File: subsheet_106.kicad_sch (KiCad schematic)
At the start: 59 parts, among them P01 1K, Q01 16MHz, T04 BC557B, T05 BC337-40, T06 BC547B, T07 BC547B, T08 BC557B, T09 BC547B, T10 BC547B

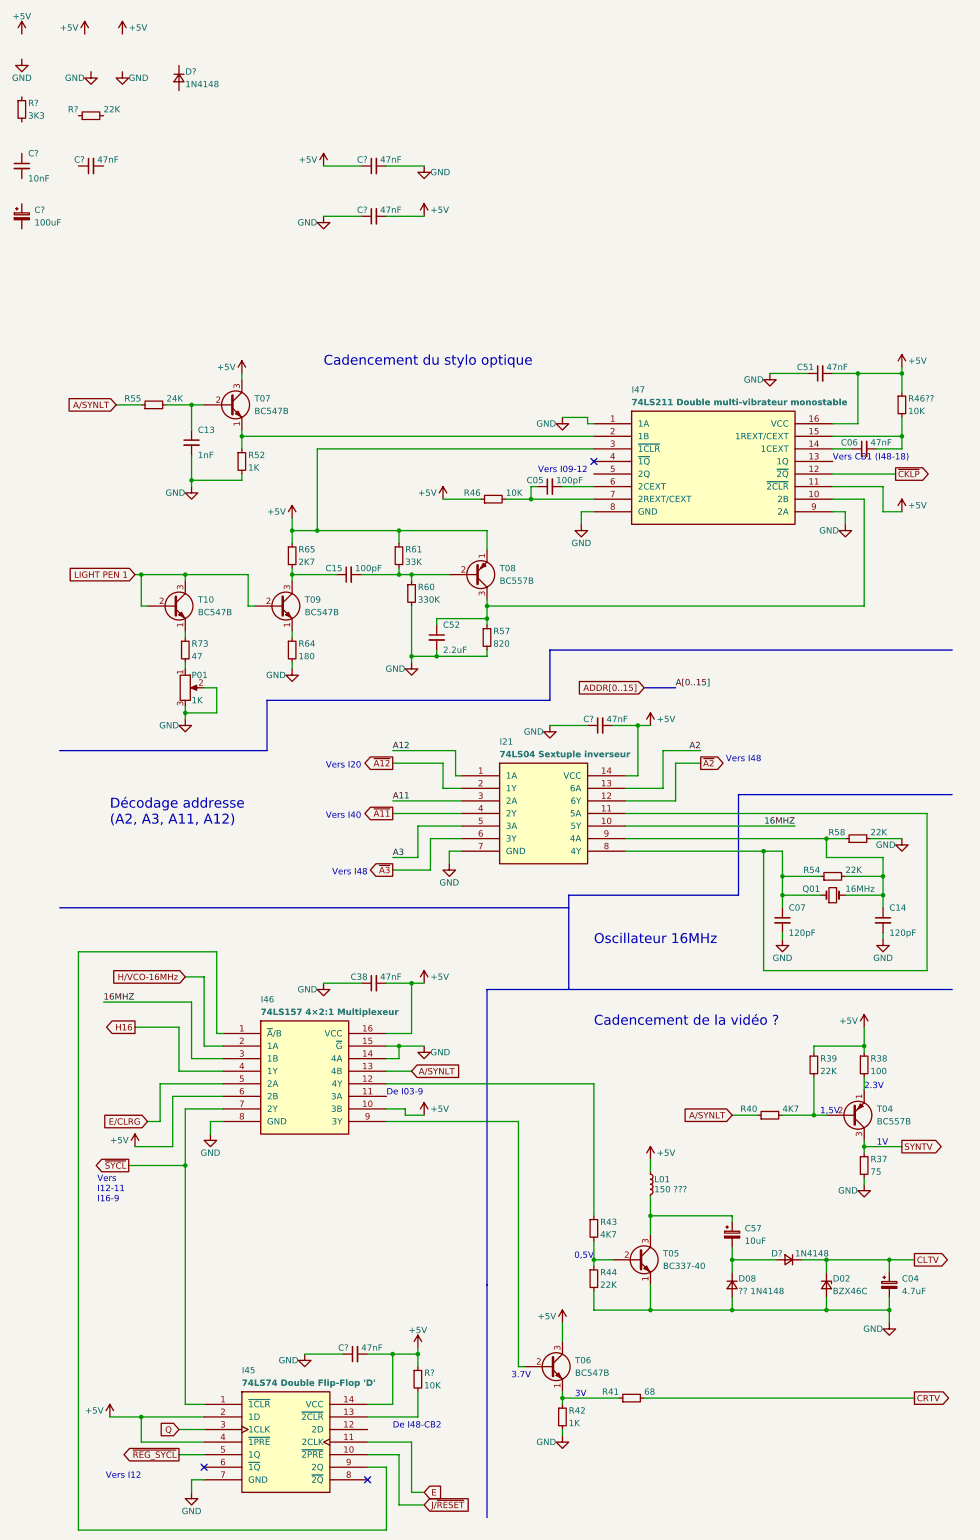
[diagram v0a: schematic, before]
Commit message: Nommage de signaux d'après documentations techniques
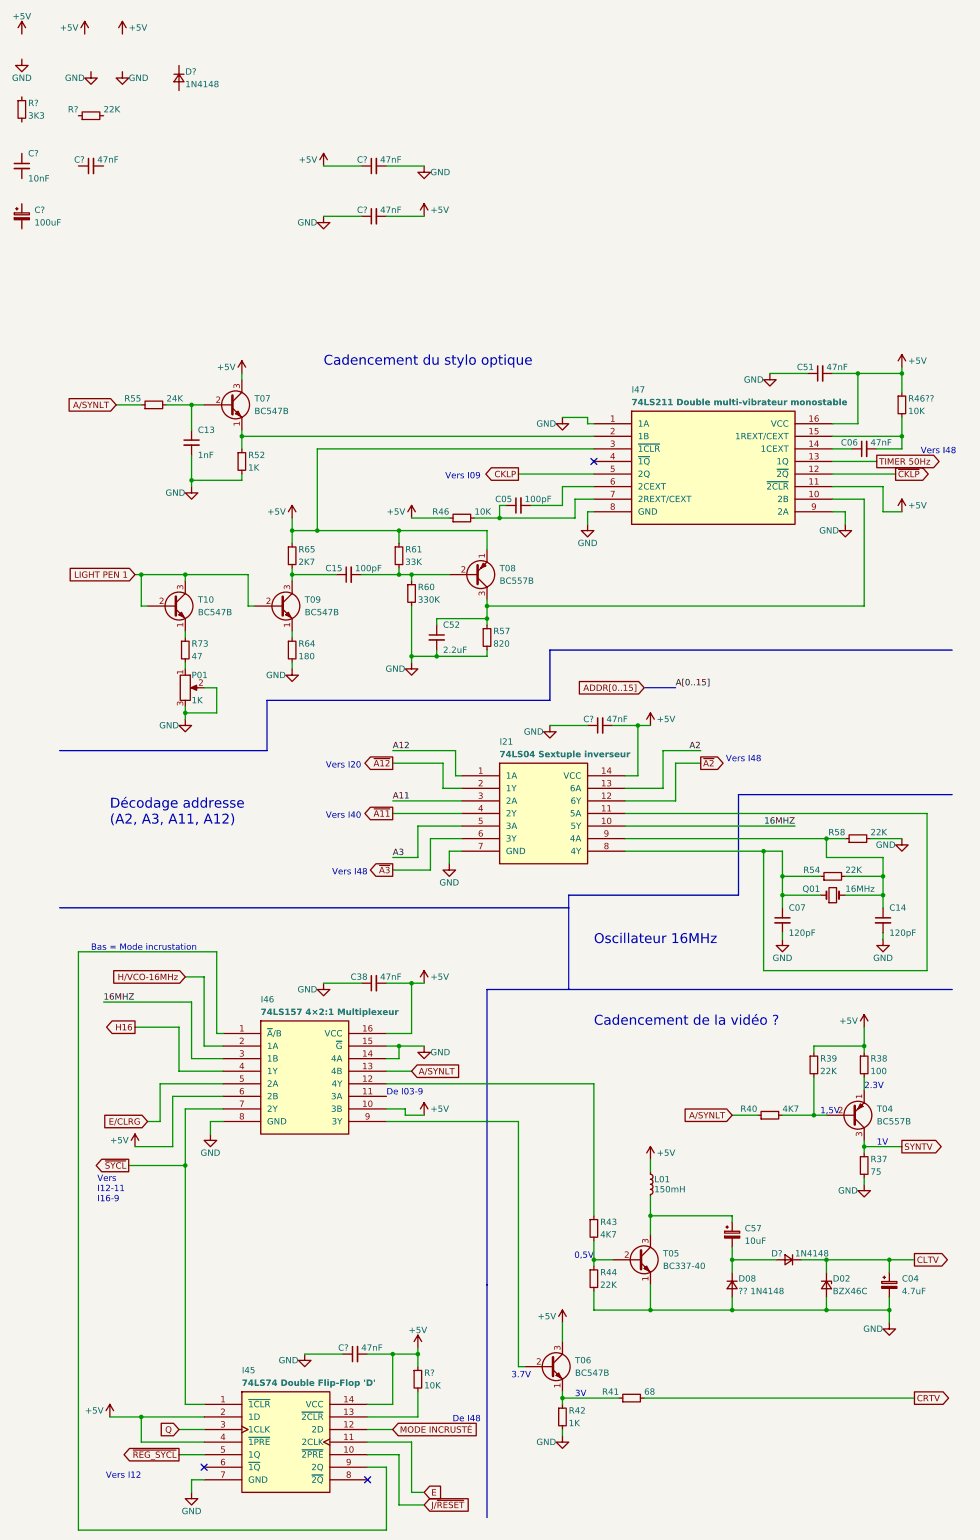
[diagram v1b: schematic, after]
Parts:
- L01: value 150 ??? -> 150mH
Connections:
- net TIMER 50Hz: now reaches I47.13 (1Q)
- net CKLP: now reaches I47.5 (2Q)
- net MODE INCRUSTÉ: now reaches I45.12 (2D)
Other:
- note added: "Bas = Mode incrustation"
- note added: "De I48"
- note added: "Vers I09"
- note removed: "De I48-CB2"
- note removed: "Vers CB1 (I48-18)"
- note removed: "Vers I09-12"
- moved on the sheet: C05, R46

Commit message: continue circuit vidéo
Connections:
- net ~{NOIR_INCR}: now reaches I46.11 (3A)
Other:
- note added: "Cadencement de la vidéo"
- note removed: "Cadencement de la vidéo ?"
- note removed: "De I03-9"
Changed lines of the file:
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@@
     (stroke (width 0) (type default) (color 0 0 0 0))
   )
-  (polyline (pts (xy 101.6 204.47) (xy 101.6 144.78))
+  (polyline (pts (xy 104.14 251.46) (xy 104.14 144.78))
     (stroke (width 0) (type default) (color 0 0 0 0))
   )
@@
     (stroke (width 0) (type default) (color 0 0 0 0))
   )
+  (wire (pts (xy 107.95 190.5) (xy 107.95 220.98))
+    (stroke (width 0) (type default) (color 0 0 0 0))
+  )
   (wire (pts (xy 92.71 104.14) (xy 96.52 104.14))
     (stroke (width 0) (type default) (color 0 0 0 0))
   )
-  (polyline (pts (xy 101.6 144.78) (xy 195.58 144.78))
+  (polyline (pts (xy 104.14 144.78) (xy 195.58 144.78))
     (stroke (width 0) (type default) (color 0 0 0 0))
   )
@@
     (stroke (width 0) (type default) (color 0 0 0 0))
   )
+  (wire (pts (xy 87.63 179.07) (xy 87.63 166.37))
+    (stroke (width 0) (type default) (color 0 0 0 0))
+  )
   (polyline (pts (xy 152.4 105.41) (xy 152.4 125.73))
     (stroke (width 0) (type default) (color 0 0 0 0))
@@
     (stroke (width 0) (type default) (color 0 0 0 0))
   )
-  (wire (pts (xy 85.09 168.91) (xy 85.09 170.18))
-    (stroke (width 0) (type default) (color 0 0 0 0))
-  )
   (wire (pts (xy 161.29 121.92) (xy 161.29 125.73))
     (stroke (width 0) (type default) (color 0 0 0 0))
@@
     (stroke (width 0) (type default) (color 0 0 0 0))
   )
+  (wire (pts (xy 82.55 171.45) (xy 82.55 190.5))
+    (stroke (width 0) (type default) (color 0 0 0 0))
+  )
   (wire (pts (xy 181.61 133.35) (xy 181.61 134.62))
     (stroke (width 0) (type default) (color 0 0 0 0))
@@
     (stroke (width 0) (type default) (color 0 0 0 0))
   )
-  (wire (pts (xy 81.28 171.45) (xy 107.95 171.45))
+  (wire (pts (xy 81.28 171.45) (xy 82.55 171.45))
     (stroke (width 0) (type default) (color 0 0 0 0))
   )
@@
     (stroke (width 0) (type default) (color 0 0 0 0))
   )
-  (wire (pts (xy 85.09 170.18) (xy 88.9 170.18))
+  (wire (pts (xy 85.09 185.42) (xy 88.9 185.42))
     (stroke (width 0) (type default) (color 0 0 0 0))
   )
@@
     (stroke (width 0) (type default) (color 0 0 0 0))
   )
+  (wire (pts (xy 81.28 166.37) (xy 87.63 166.37))
+    (stroke (width 0) (type default) (color 0 0 0 0))
+  )
   (wire (pts (xy 46.99 83.82) (xy 44.45 83.82))
     (stroke (width 0) (type default) (color 0 0 0 0))
@@
     (stroke (width 0) (type default) (color 0 0 0 0))
   )
-  (wire (pts (xy 107.95 171.45) (xy 107.95 220.98))
-    (stroke (width 0) (type default) (color 0 0 0 0))
-  )
   (wire (pts (xy 35.56 163.83) (xy 48.26 163.83))
     (stroke (width 0) (type default) (color 0 0 0 0))
@@
     (stroke (width 0) (type default) (color 0 0 0 0))
   )
+  (wire (pts (xy 88.9 179.07) (xy 87.63 179.07))
+    (stroke (width 0) (type default) (color 0 0 0 0))
+  )
   (wire (pts (xy 171.45 40.64) (xy 184.15 40.64))
     (stroke (width 0) (type default) (color 0 0 0 0))
@@
     (stroke (width 0) (type default) (color 0 0 0 0))
   )
-  (polyline (pts (xy 101.6 251.46) (xy 101.6 204.47))
-    (stroke (width 0) (type default) (color 0 0 0 0))
-  )
   (wire (pts (xy 129.54 116.84) (xy 157.48 116.84))
     (stroke (width 0) (type default) (color 0 0 0 0))
@@
     (stroke (width 0) (type default) (color 0 0 0 0))
   )
+  (wire (pts (xy 85.09 168.91) (xy 85.09 185.42))
+    (stroke (width 0) (type default) (color 0 0 0 0))
+  )
   (wire (pts (xy 116.84 227.33) (xy 116.84 228.6))
     (stroke (width 0) (type default) (color 0 0 0 0))
@@
   )
   (wire (pts (xy 52.07 20.32) (xy 52.07 21.59))
+    (stroke (width 0) (type default) (color 0 0 0 0))
+  )
+  (wire (pts (xy 82.55 190.5) (xy 107.95 190.5))
     (stroke (width 0) (type default) (color 0 0 0 0))
   )
@@
     (effects (font (size 1.27 1.27)) (justify right bottom))
   )
-  (text "Cadencement de la vidéo ?" (at 123.19 152.4 0)
+  (text "Cadencement de la vidéo" (at 123.19 152.4 0)
     (effects (font (size 2 2)) (justify left bottom))
   )
   (text "1V" (at 180.34 176.53 0)
-    (effects (font (size 1.27 1.27)) (justify left bottom))
-  )
-  (text "De I03-9" (at 81.28 166.37 0)
     (effects (font (size 1.27 1.27)) (justify left bottom))
   )
@@
     (effects (font (size 1.27 1.27)) (justify left))
     (property "Intersheet References" "${INTERSHEET_REFS}" (id 0) (at 194.9693 227.2506 0)
+      (effects (font (size 1.27 1.27)) (justify left) hide)
+    )
+  )
+  (global_label "~{NOIR_INCR}" (shape input) (at 88.9 179.07 0) (fields_autoplaced)
+    (effects (font (size 1.27 1.27)) (justify left))
+    (property "Intersheet References" "${INTERSHEET_REFS}" (id 0) (at 101.2917 178.9906 0)
       (effects (font (size 1.27 1.27)) (justify left) hide)
     )
@@
     (pin "2")
   )
-  (symbol (lib_id "power:+5V") (at 88.9 170.18 0) (unit 1)
+  (symbol (lib_id "power:+5V") (at 88.9 185.42 0) (unit 1)
     (in_bom yes) (on_board yes)
-    (property "Reference" "#PWR?" (id 0) (at 88.9 173.99 0)
-      (effects (font (size 1.27 1.27)) hide)
-    )
-    (property "Value" "+5V" (id 1) (at 90.17 168.91 0)
+    (property "Reference" "#PWR?" (id 0) (at 88.9 189.23 0)
+      (effects (font (size 1.27 1.27)) hide)
+    )
+    (property "Value" "+5V" (id 1) (at 90.17 184.15 0)
       (effects (font (size 1.27 1.27)) (justify left))
     )
-    (property "Footprint" "" (id 2) (at 88.9 170.18 0)
-      (effects (font (size 1.27 1.27)) hide)
-    )
-    (property "Datasheet" "" (id 3) (at 88.9 170.18 0)
-      (effects (font (size 1.27 1.27)) hide)
-    )
+    (property "Footprint" "" (id 2) (at 88.9 185.42 0)
+      (effects (font (size 1.27 1.27)) hide)
+    )
+    (property "Datasheet" "" (id 3) (at 88.9 185.42 0)
+      (effects (font (size 1.27 1.27)) hide)
+    )

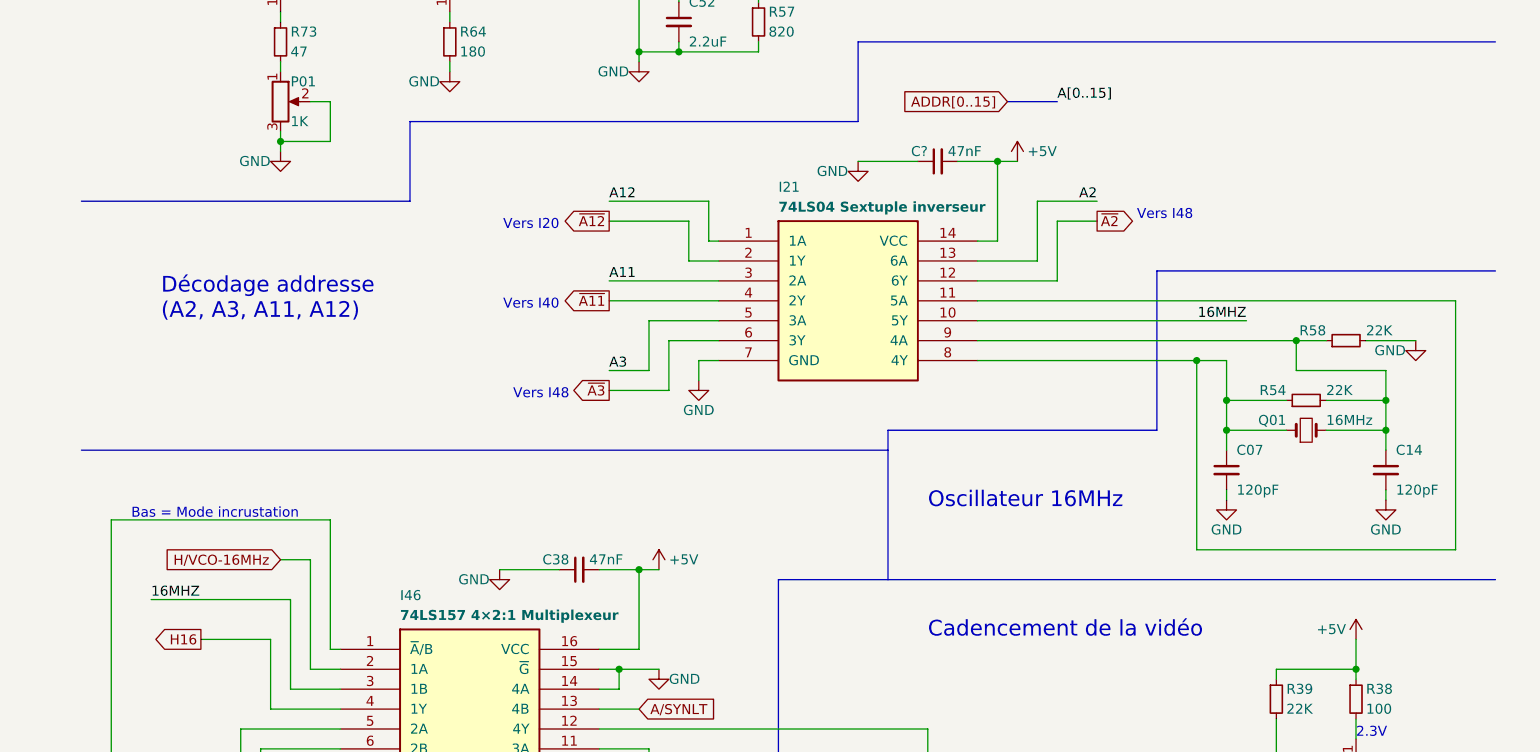
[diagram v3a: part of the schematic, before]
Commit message: bouge I21 vers la page du processeur
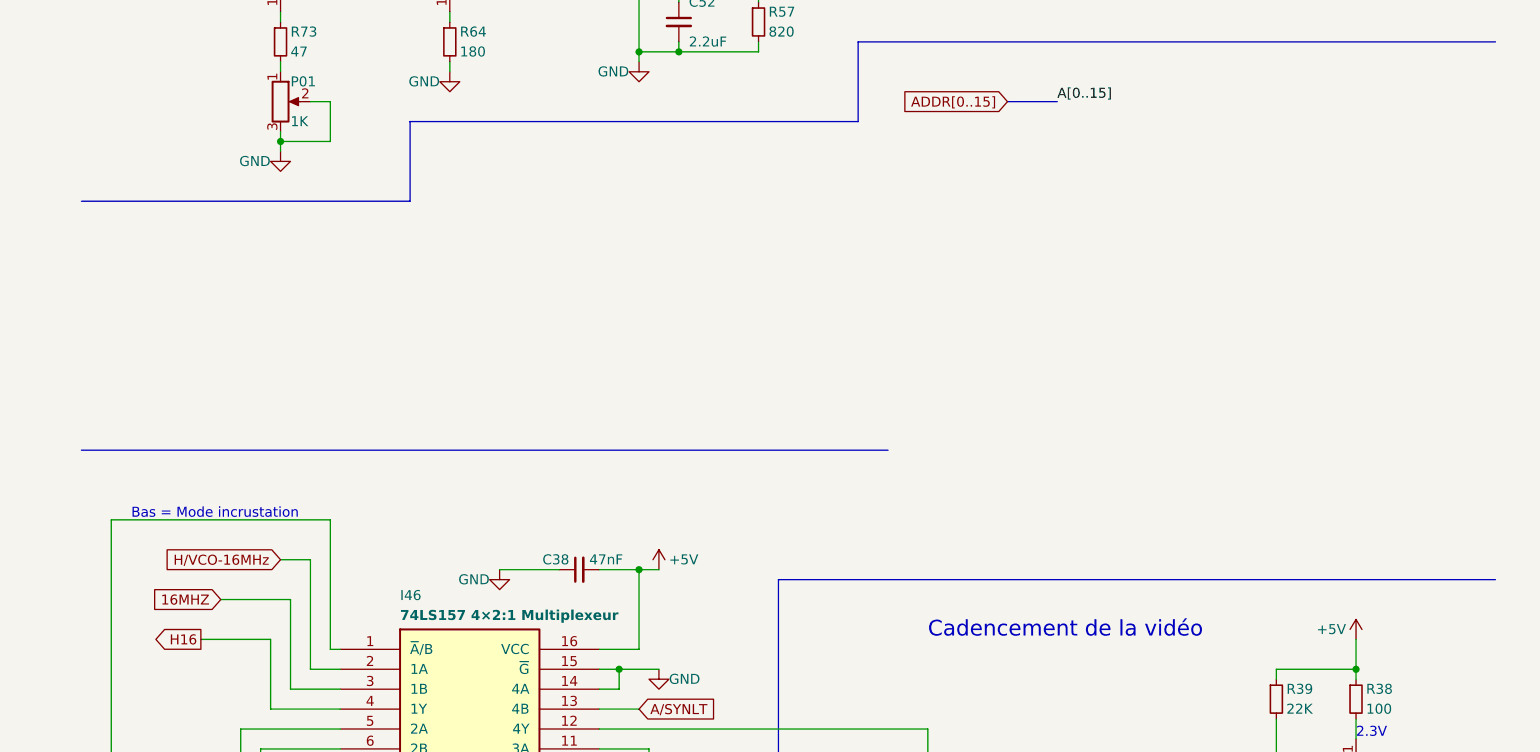
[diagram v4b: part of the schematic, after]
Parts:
- removed C07, C14: 120pF, symbol Device:C_Small
- removed C?: 47nF, symbol Device:C_Small
- removed I21: 74LS04 Sextuple inverseur, Package_DIP:DIP-14_W7.62mm_LongPads, symbol 74x04:74X04_HEX_INVERTER_PHY
- removed Q01: 16MHz, symbol Device:Crystal_Small
- removed R54, R58: 22K, symbol Device:R_Small
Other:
- note removed: "Décodage addresse (A2, A3, A11, A12)"
- note removed: "Oscillateur 16MHz"
- note removed: "Vers I20"
- note removed: "Vers I40"
